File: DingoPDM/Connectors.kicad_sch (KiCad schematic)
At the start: 13 parts, among them J1 RedCubeTerminal, J2 USB_C_Receptacle_USB2.0, J3 DTM1312PA12PBR008, Q1 BC817-40

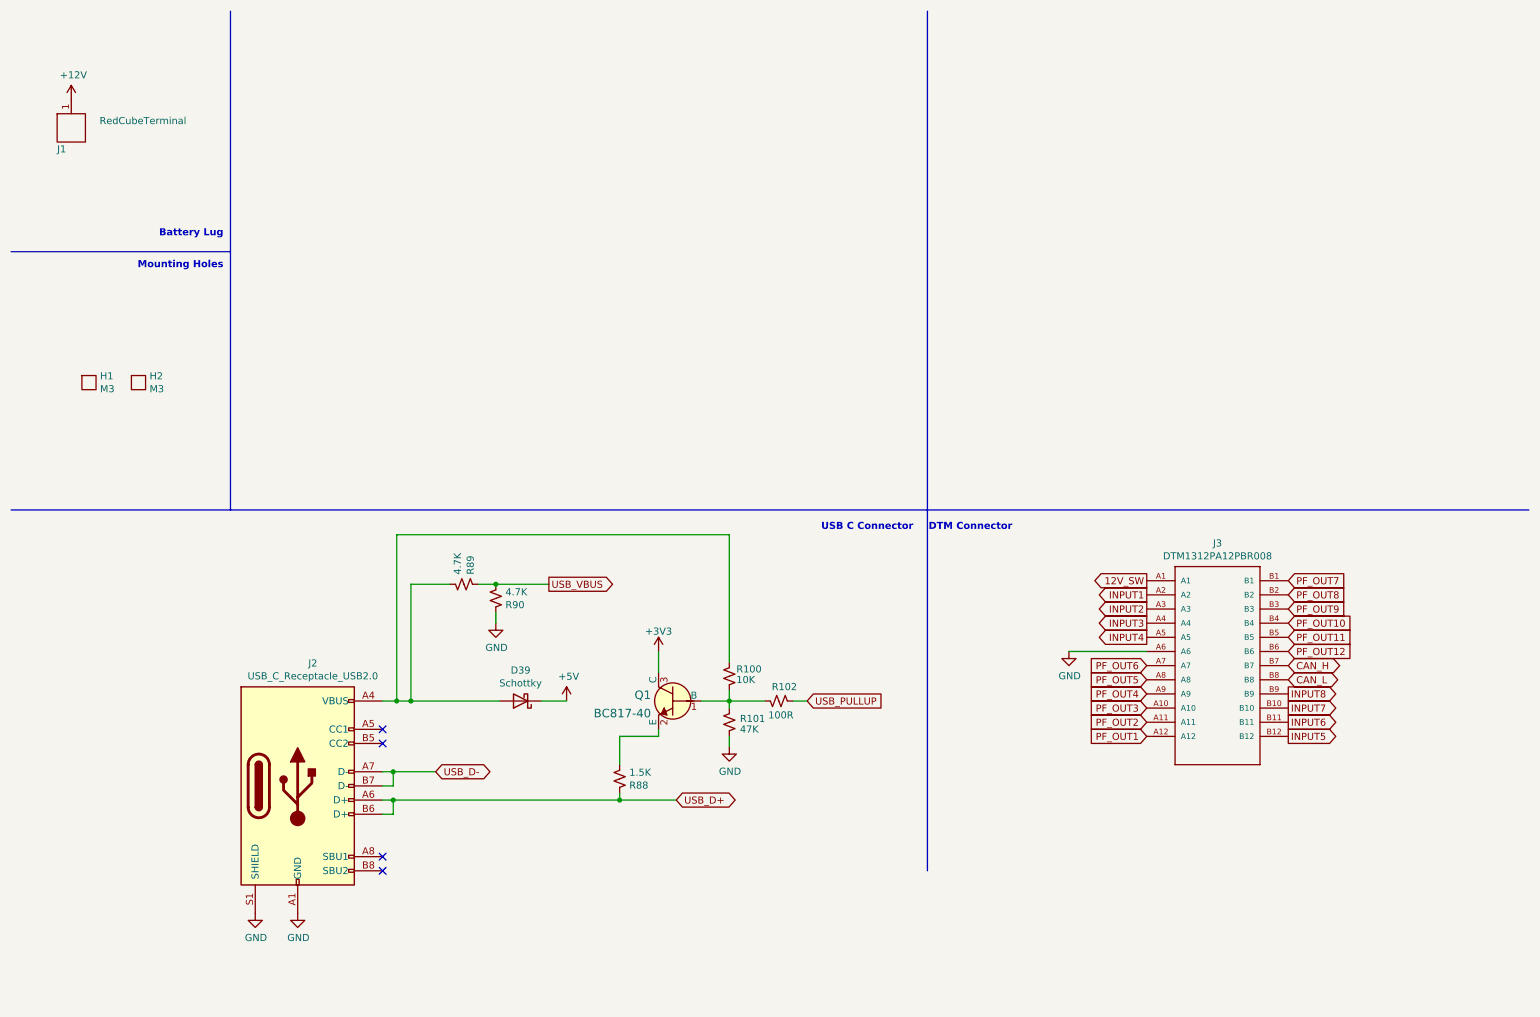
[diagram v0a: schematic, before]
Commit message: Swapped to AMPSEAL 14 pins
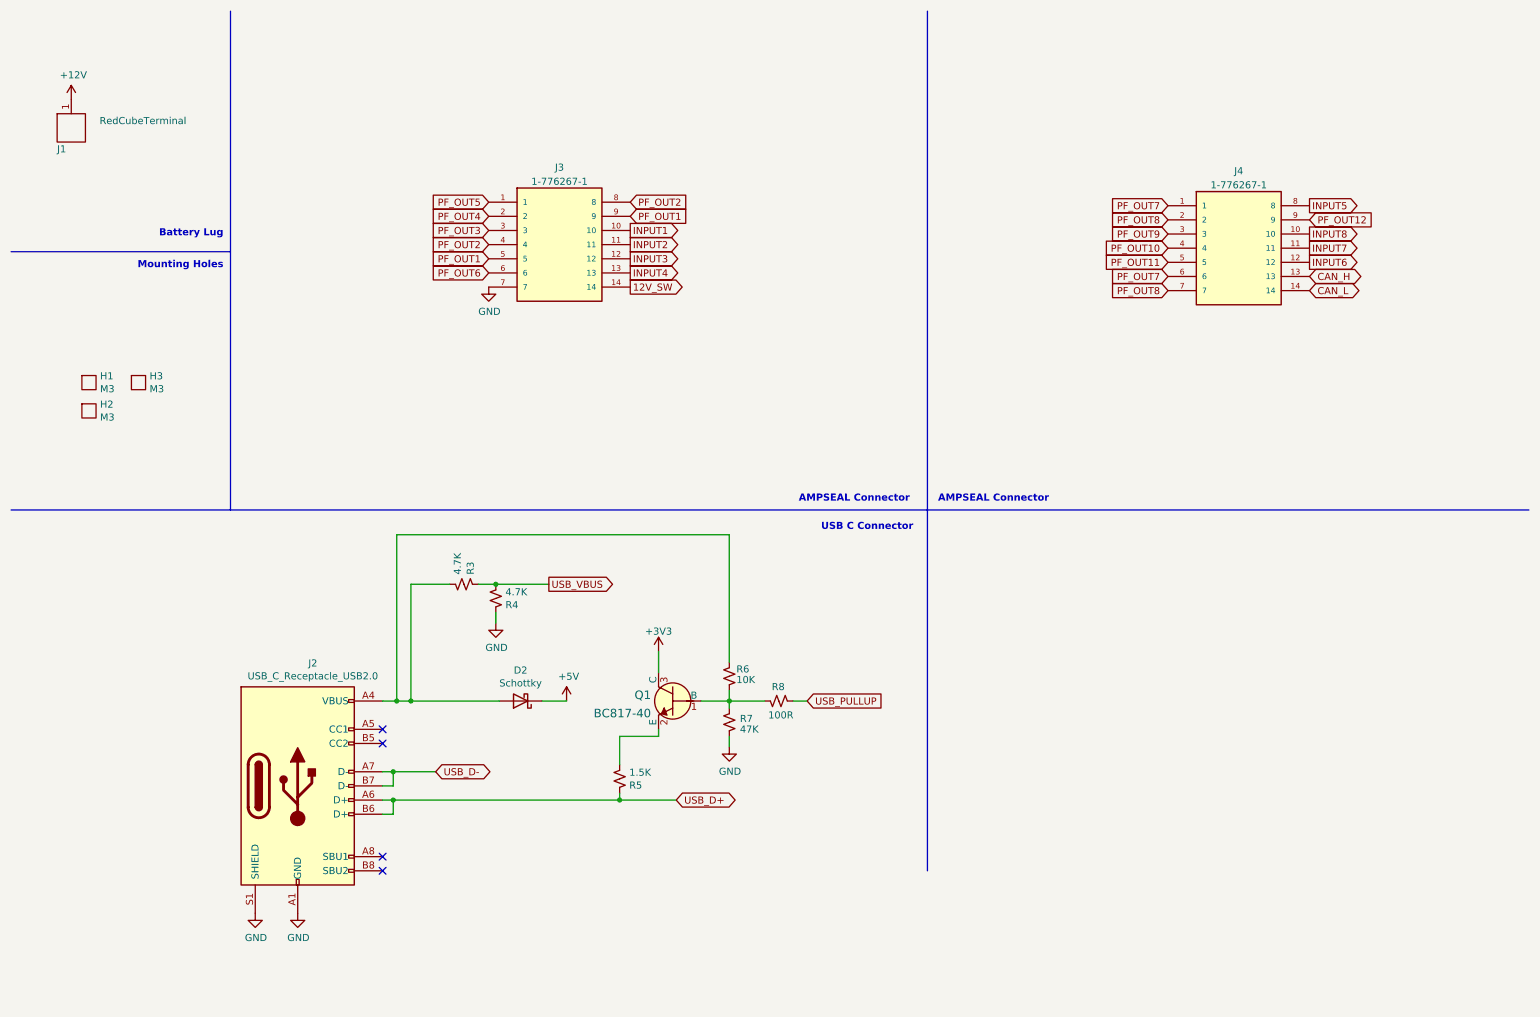
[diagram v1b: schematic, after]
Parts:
- removed J3: DTM1312PA12PBR008, Deutsch_DTM:TE_DTM1312PA12PBR008, symbol Deutsch_DTM:DTM1312PA12PBR008
- added H2: M3, MountingHole:MountingHole_3mm_Pad, symbol DingoPDM-rescue:M3-MountingHoles
- added J3, J4: 1-776267-1, AMPSeal:AMPSeal_14Pin_Horiz_NoHoles, symbol AMPSeal:AMPSeal_14Pin
- renumbered D39 to D2, H2 to H3, R89 to R3, R90 to R4, R88 to R5, R100 to R6, R101 to R7, R102 to R8
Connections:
- net 12V_SW: now also J3.14
- net CAN_H: now also J4.13
- net CAN_L: now also J4.14
- net GND: now also J3.7
- net INPUT1: now also J3.10
- net INPUT2: now also J3.11
- net INPUT3: now also J3.12
- net INPUT4: now also J3.13
- net INPUT5: now also J4.8
- net INPUT6: now also J4.12
- net INPUT7: now also J4.11
- net INPUT8: now also J4.10
- net PF_OUT1: now also J3.5, J3.9
- net PF_OUT10: now also J4.4
- net PF_OUT11: now also J4.5
- net PF_OUT12: now also J4.9
- net PF_OUT2: now also J3.4, J3.8
- net PF_OUT3: now also J3.3
- net PF_OUT4: now also J3.2
- net PF_OUT5: now also J3.1
- net PF_OUT6: now also J3.6
- net PF_OUT7: now also J4.1, J4.6
- net PF_OUT8: now also J4.2, J4.7
- net PF_OUT9: now also J4.3
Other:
- note added: "AMPSEAL Connector"
- note removed: "DTM Connector"

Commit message: layout finished
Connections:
- net 12V_SW renamed ON_SW
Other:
- note added: "A"
- note added: "B"
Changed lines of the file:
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@@
     (stroke (width 0) (type default) (color 0 0 0 0))
+  )
+  (text "B" (at 231.775 67.945 0)
+    (effects (font (size 1.27 1.27)) (justify left bottom))
+  )
+  (text "A" (at 109.855 67.945 0)
+    (effects (font (size 1.27 1.27)) (justify left bottom))
   )
   (text "AMPSEAL Connector" (at 178.435 100.33 0)
@@
     )
   )
-  (global_label "12V_SW" (shape output) (at 123.19 61.595 0) (fields_autoplaced)
+  (global_label "ON_SW" (shape output) (at 123.19 61.595 0) (fields_autoplaced)
     (effects (font (size 1.27 1.27)) (justify left))
-    (property "Intersheet References" "${INTERSHEET_REFS}" (id 0) (at 339.09 175.895 0)
-      (effects (font (size 1.27 1.27)) hide)
+    (property "Intersheet References" "${INTERSHEET_REFS}" (id 0) (at 131.8037 61.5156 0)
+      (effects (font (size 1.27 1.27)) (justify left) hide)
     )
   )

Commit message: Added export, fixed some PNs
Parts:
- J3, J4: Digi-Key_PN (none) -> A142413-ND
- R8: Digi-Key_PN 311-4.70KCRCT-ND -> 311-100CRCT-ND
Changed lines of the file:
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@@
       (effects (font (size 1.27 1.27)) (justify left bottom) hide)
+    )
+    (property "Digi-Key_PN" "A142413-ND" (id 4) (at 110.49 53.975 0)
+      (effects (font (size 1.27 1.27)) hide)
     )
     (pin "1")
@@
       (effects (font (size 1.27 1.27)) (justify left bottom) hide)
     )
+    (property "Digi-Key_PN" "A142413-ND" (id 4) (at 232.41 54.61 0)
+      (effects (font (size 1.27 1.27)) hide)
+    )
     (pin "1")
     (pin "10")
@@
       (effects (font (size 1.27 1.27)) hide)
     )
-    (property "Digi-Key_PN" "311-4.70KCRCT-ND" (id 4) (at 149.86 135.89 0)
+    (property "Digi-Key_PN" "311-100CRCT-ND" (id 4) (at 149.86 135.89 0)
       (effects (font (size 1.27 1.27)) hide)
     )

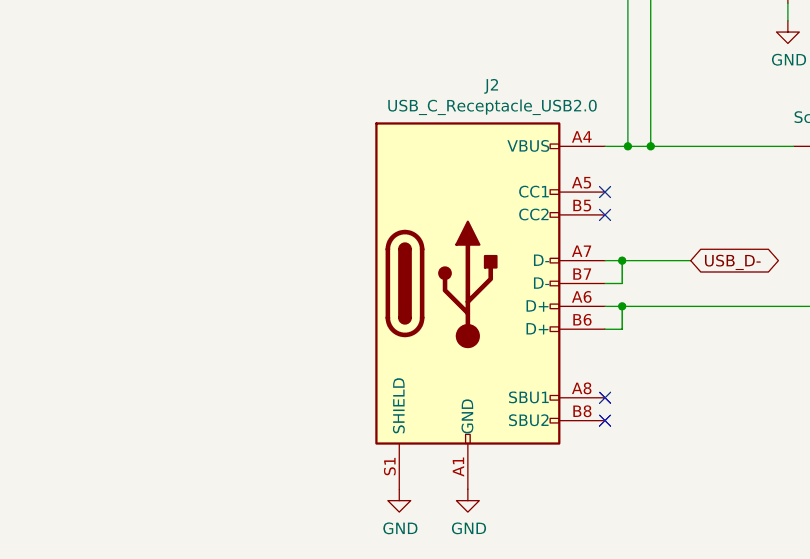
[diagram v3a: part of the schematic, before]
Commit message: V5 changes
Changed tracks/clearances/DRC to meet JLCPCB 2oz rules. Changed on switch to 12V input. Switched to TagConnect
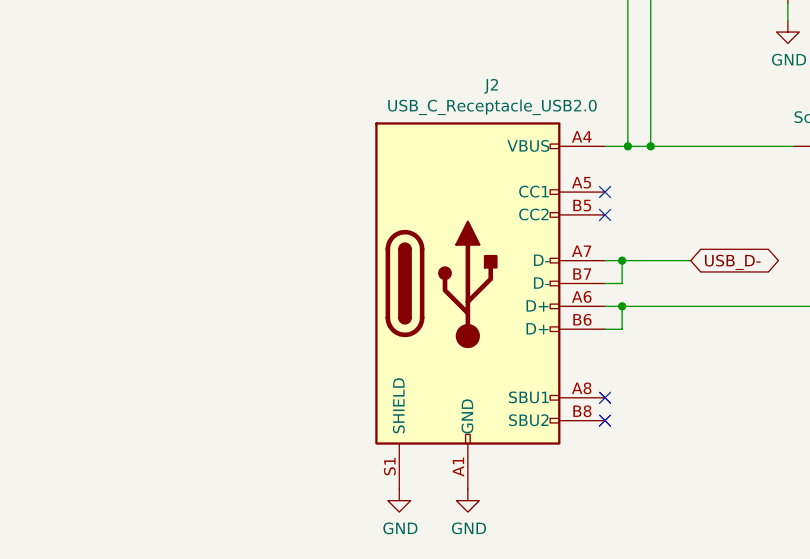
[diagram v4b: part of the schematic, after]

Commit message: Documentation cleanup
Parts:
- Q1: Category Discrete Semiconductor Products -> (none); DK_Datasheet_Link https://assets.nexperia.com/documents/data-sheet/BC817_SER.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 -> (none); DK_Detail_Page /product-detail/en/nexperia-usa-inc/BC817-40,215/1727-2919-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 -> (none); Family Transistors - Bipolar (BJT) - Single -> (none); MPN BC817-40,215 -> (none); Manufacturer Nexperia USA Inc. -> (none); Status Active -> (none)
- R3, R4: value 4.7K -> 4.7k
- R5: value 1.5K -> 1.5k
- R6: value 10K -> 10k; Digi-Key_PN 311-4.70KCRCT-ND -> 311-10.0KCRDKR-ND
- R7: value 47K -> 47k; Digi-Key_PN 311-4.70KCRCT-ND -> 311-47.0KCRCT-ND
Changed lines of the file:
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@@
       (effects (font (size 1.27 1.27)) hide)
     )
-    (property "Datasheet" "~" (at 103.505 135.89 0)
+    (property "Datasheet" "" (at 103.505 135.89 0)
       (effects (font (size 1.27 1.27)) hide)
     )
@@
       (effects (font (size 1.27 1.27)) (justify left))
     )
-    (property "Value" "1.5K" (at 123.0122 148.717 0)
+    (property "Value" "1.5k" (at 123.0122 148.717 0)
       (effects (font (size 1.27 1.27)) (justify left))
     )
@@
       (effects (font (size 1.27 1.27)) hide)
     )
-    (property "Datasheet" "~" (at 121.285 149.86 0)
+    (property "Datasheet" "" (at 121.285 149.86 0)
       (effects (font (size 1.27 1.27)) hide)
     )
@@
       (effects (font (size 1.27 1.27)) (justify left))
     )
-    (property "Value" "4.7K" (at 100.7872 116.332 0)
+    (property "Value" "4.7k" (at 100.7872 116.332 0)
       (effects (font (size 1.27 1.27)) (justify left))
     )
@@
       (effects (font (size 1.27 1.27)) hide)
     )
-    (property "Datasheet" "~" (at 99.06 117.475 0)
+    (property "Datasheet" "" (at 99.06 117.475 0)
       (effects (font (size 1.27 1.27)) hide)
     )
@@
       (effects (font (size 1.27 1.27)) (justify left))
     )
-    (property "Value" "4.7K" (at 92.202 113.2078 0)
+    (property "Value" "4.7k" (at 92.202 113.2078 0)
       (effects (font (size 1.27 1.27)) (justify left))
     )
@@
       (effects (font (size 1.27 1.27)) hide)
     )
-    (property "Datasheet" "~" (at 93.345 114.935 0)
+    (property "Datasheet" "" (at 93.345 114.935 0)
       (effects (font (size 1.27 1.27)) hide)
     )
@@
       (effects (font (size 1.27 1.27)) hide)
     )
-    (property "Datasheet" "https://www.usb.org/sites/default/files/documents/usb_type-c.zip" (at 67.31 151.13 0)
+    (property "Datasheet" "" (at 67.31 151.13 0)
       (effects (font (size 1.27 1.27)) hide)
     )
@@
       (effects (font (size 1.27 1.27)) (justify left))
     )
-    (property "Value" "47K" (at 142.875 140.97 0)
+    (property "Value" "47k" (at 142.875 140.97 0)
       (effects (font (size 1.27 1.27)) (justify left))
     )
@@
       (effects (font (size 1.27 1.27)) hide)
     )
-    (property "Datasheet" "~" (at 140.97 139.7 0)
-      (effects (font (size 1.27 1.27)) hide)
-    )
-    (property "Digi-Key_PN" "311-4.70KCRCT-ND" (at 140.97 139.7 0)
+    (property "Datasheet" "" (at 140.97 139.7 0)
+      (effects (font (size 1.27 1.27)) hide)
+    )
+    (property "Digi-Key_PN" "311-47.0KCRCT-ND" (at 140.97 139.7 0)
       (effects (font (size 1.27 1.27)) hide)
     )
@@
       (effects (font (size 1.524 1.524)) (justify left) hide)
     )
-    (property "Datasheet" "https://assets.nexperia.com/documents/data-sheet/BC817_SER.pdf" (at 125.73 128.27 0)
+    (property "Datasheet" "" (at 125.73 128.27 0)
       (effects (font (size 1.524 1.524)) (justify left) hide)
     )
     (property "Digi-Key_PN" "1727-2919-1-ND" (at 125.73 125.73 0)
-      (effects (font (size 1.524 1.524)) (justify left) hide)
-    )
-    (property "MPN" "BC817-40,215" (at 125.73 123.19 0)
-      (effects (font (size 1.524 1.524)) (justify left) hide)
-    )
-    (property "Category" "Discrete Semiconductor Products" (at 125.73 120.65 0)
-      (effects (font (size 1.524 1.524)) (justify left) hide)
-    )
-    (property "Family" "Transistors - Bipolar (BJT) - Single" (at 125.73 118.11 0)
-      (effects (font (size 1.524 1.524)) (justify left) hide)
-    )
-    (property "DK_Datasheet_Link" "https://assets.nexperia.com/documents/data-sheet/BC817_SER.pdf" (at 125.73 115.57 0)
-      (effects (font (size 1.524 1.524)) (justify left) hide)
-    )
-    (property "DK_Detail_Page" "/product-detail/en/nexperia-usa-inc/BC817-40,215/1727-2919-1-ND/763458" (at 125.73 113.03 0)
-      (effects (font (size 1.524 1.524)) (justify left) hide)
-    )
-    (property "Description" "TRANS NPN 45V 0.5A SOT23" (at 125.73 110.49 0)
-      (effects (font (size 1.524 1.524)) (justify left) hide)
-    )
-    (property "Manufacturer" "Nexperia USA Inc." (at 125.73 107.95 0)
-      (effects (font (size 1.524 1.524)) (justify left) hide)
-    )
-    (property "Status" "Active" (at 125.73 105.41 0)
       (effects (font (size 1.524 1.524)) (justify left) hide)
     )
@@
       (effects (font (size 1.27 1.27)) (justify left))
     )
-    (property "Value" "10K" (at 142.24 132.08 0)
+    (property "Value" "10k" (at 142.24 132.08 0)
       (effects (font (size 1.27 1.27)) (justify left))
     )
@@
       (effects (font (size 1.27 1.27)) hide)
     )
-    (property "Datasheet" "~" (at 140.97 131.445 0)
-      (effects (font (size 1.27 1.27)) hide)
-    )
-    (property "Digi-Key_PN" "311-4.70KCRCT-ND" (at 140.97 131.445 0)
+    (property "Datasheet" "" (at 140.97 131.445 0)
+      (effects (font (size 1.27 1.27)) hide)
+    )
+    (property "Digi-Key_PN" "311-10.0KCRDKR-ND" (at 140.97 131.445 0)
       (effects (font (size 1.27 1.27)) hide)
     )
@@
       (effects (font (size 1.27 1.27)) hide)
     )
-    (property "Datasheet" "~" (at 149.86 135.89 0)
-      (effects (font (size 1.27 1.27)) hide)
-    )
+    (property "Datasheet" "" (at 149.86 135.89 0)
+      (effects (font (size 1.27 1.27)) hide)
+    )

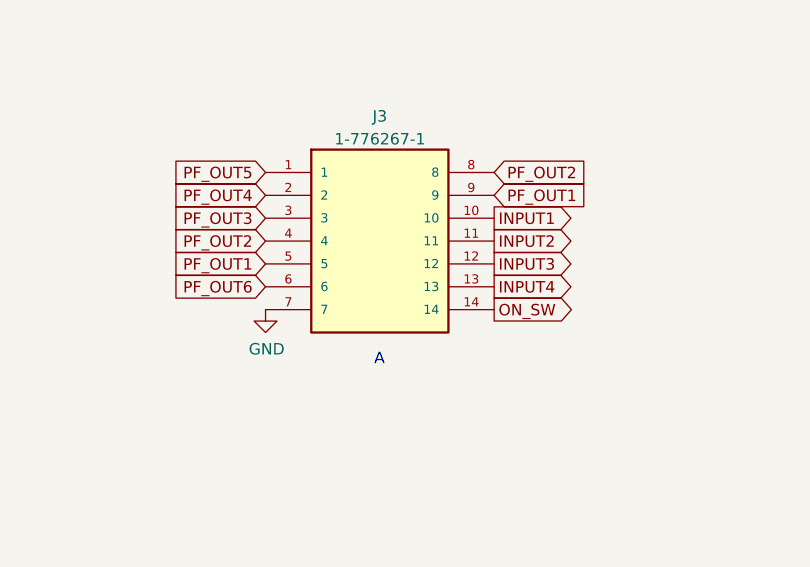
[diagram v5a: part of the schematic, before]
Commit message: V5 As Built
-Changed ADS1015 to MAX11613EUA+T due to supply issues
-Changed PCB to match JLCPCB 2oz rules
-Changed ON_SW input to 12V switched
-Switched to TagConnect TC2030
-Changed pin positions of GND, IN1, IN2
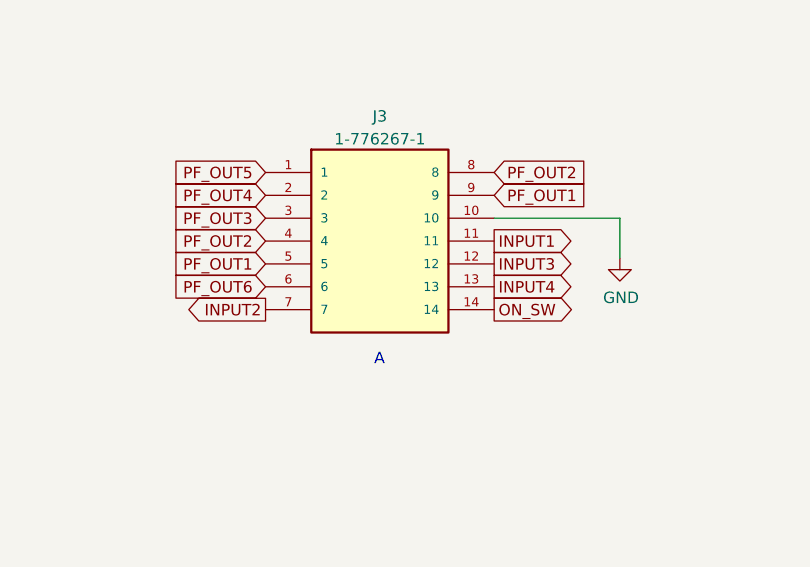
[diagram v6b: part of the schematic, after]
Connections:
- net GND: now also J3.10; no longer J3.7
- net INPUT1: now also J3.11; no longer J3.10
- net INPUT2: now also J3.7; no longer J3.11
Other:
- title: (none) -> Dingo_PDM
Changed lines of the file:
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@@
 (kicad_sch (version 20230121) (generator eeschema)
   (paper "A4")
+  (title_block
+    (title "Dingo_PDM")
+    (date "2023-02-23")
+    (rev "v5")
+    (comment 3 "github.com/corygrant")
+    (comment 4 "Cory Grant")
+  )
   (junction (at 80.645 148.59) (diameter 0) (color 0 0 0 0)
   )
@@
     (stroke (width 0) (type default))
   )
+  (wire (pts (xy 123.19 51.435) (xy 137.16 51.435))
+    (stroke (width 0) (type default))
+  )
   (wire (pts (xy 80.645 153.67) (xy 121.285 153.67))
     (stroke (width 0) (type default))
@@
   )
   (wire (pts (xy 140.97 133.985) (xy 140.97 135.89))
+    (stroke (width 0) (type default))
+  )
+  (wire (pts (xy 137.16 51.435) (xy 137.16 55.88))
     (stroke (width 0) (type default))
   )
@@
     )
   )
-  (global_label "INPUT2" (shape output) (at 123.19 53.975 0) (fields_autoplaced)
-    (effects (font (size 1.27 1.27)) (justify left))
-    (property "Intersheetrefs" "${INTERSHEET_REFS}" (at 339.09 173.355 0)
-      (effects (font (size 1.27 1.27)) hide)
+  (global_label "INPUT2" (shape output) (at 97.79 61.595 180) (fields_autoplaced)
+    (effects (font (size 1.27 1.27)) (justify right))
+    (property "Intersheetrefs" "${INTERSHEET_REFS}" (at 88.8255 61.595 0)
+      (effects (font (size 1.27 1.27)) (justify right) hide)
     )
   )
@@
     )
   )
-  (global_label "INPUT1" (shape output) (at 123.19 51.435 0) (fields_autoplaced)
-    (effects (font (size 1.27 1.27)) (justify left))
-    (property "Intersheetrefs" "${INTERSHEET_REFS}" (at 339.09 168.275 0)
+  (global_label "INPUT1" (shape output) (at 123.19 53.975 0) (fields_autoplaced)
+    (effects (font (size 1.27 1.27)) (justify left))
+    (property "Intersheetrefs" "${INTERSHEET_REFS}" (at 339.09 170.815 0)
       (effects (font (size 1.27 1.27)) hide)
     )
@@
     )
   )
-  (symbol (lib_id "power:GND") (at 97.79 61.595 0) (unit 1)
-    (in_bom yes) (on_board yes) (dnp no)
-    (property "Reference" "#PWR08" (at 97.79 67.945 0)
-      (effects (font (size 1.27 1.27)) hide)
-    )
-    (property "Value" "GND" (at 97.917 65.9892 0)
-      (effects (font (size 1.27 1.27)))
-    )
-    (property "Footprint" "" (at 97.79 61.595 0)
-      (effects (font (size 1.27 1.27)) hide)
-    )
-    (property "Datasheet" "" (at 97.79 61.595 0)
-      (effects (font (size 1.27 1.27)) hide)
-    )
+  (symbol (lib_id "power:GND") (at 137.16 55.88 0) (unit 1)
+    (in_bom yes) (on_board yes) (dnp no)
+    (property "Reference" "#PWR08" (at 137.16 62.23 0)
+      (effects (font (size 1.27 1.27)) hide)
+    )
+    (property "Value" "GND" (at 137.287 60.2742 0)
+      (effects (font (size 1.27 1.27)))
+    )
+    (property "Footprint" "" (at 137.16 55.88 0)
+      (effects (font (size 1.27 1.27)) hide)
+    )
+    (property "Datasheet" "" (at 137.16 55.88 0)
+      (effects (font (size 1.27 1.27)) hide)
+    )
